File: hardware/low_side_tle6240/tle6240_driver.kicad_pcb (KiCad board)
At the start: 2 copper layers, 58.4 x 50.8 mm, 17 parts, among them K1 CONN_3, P1 CONN_10X2, P2 CONN_2, P3 CONN_4, P4 CONN_4, P5 CONN_4, P6 CONN_4

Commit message: v2
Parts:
- removed ? (x4): , 1pin
- removed P4, P5, P6: CONN_4, bornier4
- added K2: CONN_3, bornier3, F.Cu at (197.5, 97.2)
- added R3: R, SM0805, F.Cu at (186.7, 105.4)
- P2: value CONN_2 -> CONN_16; footprint bornier2 -> SIL-16_3.5MM
- P3: value CONN_4 -> CONN_2X2; footprint bornier4 -> PIN_ARRAY_2X2
- moved P2 130.4 mm to (217.2, 121.9), turned to 270 degrees
- moved C1 130.3 mm to (211.5, 142.2)
- moved K1 123.9 mm to (208.9, 143.5), turned to 90 degrees
- moved P3 102.9 mm to (195.6, 108.0), turned to 0 degrees
- moved R1 100.8 mm to (193.7, 102.9)
- moved D1 98.6 mm to (186.7, 103.5)
- moved D2 98.4 mm to (198.8, 132.1), turned to 180 degrees
- moved P1 72.6 mm to (179.1, 138.4)
- moved R2 54.3 mm to (188.0, 109.9), turned to 270 degrees
- moved D3 49.5 mm to (186.7, 107.3), turned to 0 degrees
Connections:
- D3 pad 1: N-0000034 -> +5V
- D3 pad 2: /Fault -> N-0000015
- P1 pad 1: +5V -> GND
- P1 pad 10: /SCLK -> /IN2
- P1 pad 11: /SO -> (no net)
- P1 pad 12: /CS -> /IN1
- P1 pad 13: /Reset -> (no net)
- P1 pad 14: /PRG -> /IN9
- P1 pad 15: /Fault -> /CS
- P1 pad 16: (no net) -> /IN10
- P1 pad 17: /IN4 -> /IN3
- P1 pad 18: /IN3 -> /IN11
- P1 pad 19: /IN10 -> /IN4
- P1 pad 2: +5V -> GND
- P1 pad 20: /IN9 -> /IN12
- P1 pad 3: GND -> +5V
- P1 pad 4: GND -> +5V
- P1 pad 5: /IN12 -> /+3.3V
- P1 pad 6: /IN11 -> /+3.3V
- P1 pad 7: /IN2 -> (no net)
- P1 pad 8: /IN1 -> (no net)
- P1 pad 9: /SI -> (no net)
- P2 pad 1: +5V -> /OUT6
- P2 pad 2: GND -> /OUT5
- P3 pad 1: /OUT9 -> /SI
- P3 pad 2: /OUT10 -> /Reset
- P3 pad 3: /OUT1 -> /SO
- P3 pad 4: /OUT2 -> /SCLK
- R2 pad 1: N-0000034 -> N-0000015
- R2 pad 2: +5V -> /Fault
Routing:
- net /+3.3V: track 0.00 -> 48.3 mm
- net /PRG: track 55.4 -> 17.0 mm, vias 1 -> 0
- net GND: track 118.4 -> 150.6 mm, vias 4 -> 3
- net /OUT6: track 24.3 -> 55.9 mm
- net /OUT5: track 21.2 -> 52.2 mm
- net /SCLK: track 18.3 -> 48.2 mm, vias 0 -> 1
- net /OUT16: track 19.2 -> 49.0 mm
- net /OUT14: track 19.1 -> 48.5 mm
- net /OUT15: track 19.1 -> 47.6 mm
- net /OUT8: track 21.2 -> 48.0 mm
- net /SI: track 15.2 -> 41.3 mm, vias 0 -> 1
- net /OUT13: track 19.2 -> 44.7 mm
- net /IN4: track 40.7 -> 66.1 mm
- net /OUT7: track 24.3 -> 48.5 mm
- net /SO: track 15.5 -> 37.8 mm, vias 0 -> 1
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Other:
- board size 58.4 x 50.8 mm -> 47 x 58.9 mm
- net class Power added: clearance 0.154, trace_width 0.4, via_dia 0.889, via_drill 0.635
- net class power removed
- board text removed: "+ -"
- board text removed: "Fault"
- board text removed: "OUT1"
- board text removed: "OUT10"
- board text removed: "OUT11"
- board text removed: "OUT12"
- board text removed: "OUT13"
- board text removed: "OUT14"
- board text removed: "OUT15"
- board text removed: "OUT16"
- board text removed: "OUT2"
- board text removed: "OUT3"
- board text removed: "OUT4"
- board text removed: "OUT5"
- board text removed: "OUT6"
- board text removed: "OUT7"
- board text removed: "OUT8"
- board text removed: "OUT9"
- board text removed: "Power"
- board text removed: "Prg"

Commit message: 
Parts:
- K1: value CONN_3 -> JUMPER3
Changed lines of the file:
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@@
   (net 33 /SO)
   (net 34 GND)
-  (net 35 N-0000015)
-  (net 36 N-0000017)
+  (net 35 N-0000014)
+  (net 36 N-0000023)
   (net_class Default "This is the default net class."
     (clearance 0)
@@
     (uvia_drill 0.127)
     (add_net "")
+    (add_net N-0000014)
+    (add_net N-0000023)
   )
   (net_class Power ""
@@
     (add_net /SI)
     (add_net /SO)
-    (add_net N-0000015)
-    (add_net N-0000017)
   )
   (module SM0805 (layer F.Cu)
@@
     (pad 2 smd rect (at 0.9525 0 180) (size 0.889 1.397)
       (layers F.Cu F.Paste F.Mask)
-      (net 36 N-0000017)
+      (net 36 N-0000023)
     )
     (model smd/chip_cms.wrl
@@
     (pad 1 smd rect (at -0.9525 0 270) (size 0.889 1.397)
       (layers F.Cu F.Paste F.Mask)
-      (net 35 N-0000015)
+      (net 35 N-0000014)
     )
     (pad 2 smd rect (at 0.9525 0 270) (size 0.889 1.397)
@@
       (effects (font (size 1.016 1.016) (thickness 0.1524)))
     )
-    (fp_text value CONN_3 (at 0 -2.159 90) (layer F.SilkS) hide
+    (fp_text value JUMPER3 (at 0 -2.159 90) (layer F.SilkS) hide
       (effects (font (size 1.016 1.016) (thickness 0.1524)))
     )
@@
     (pad 2 smd rect (at 1.04902 0) (size 1.19888 1.19888)
       (layers F.Cu F.Paste F.Mask)
-      (net 36 N-0000017)
+      (net 36 N-0000023)
     )
   )
@@
     (pad 2 smd rect (at 1.04902 0) (size 1.19888 1.19888)
       (layers F.Cu F.Paste F.Mask)
-      (net 35 N-0000015)
-    )
-  )
+      (net 35 N-0000014)
+    )
+  )

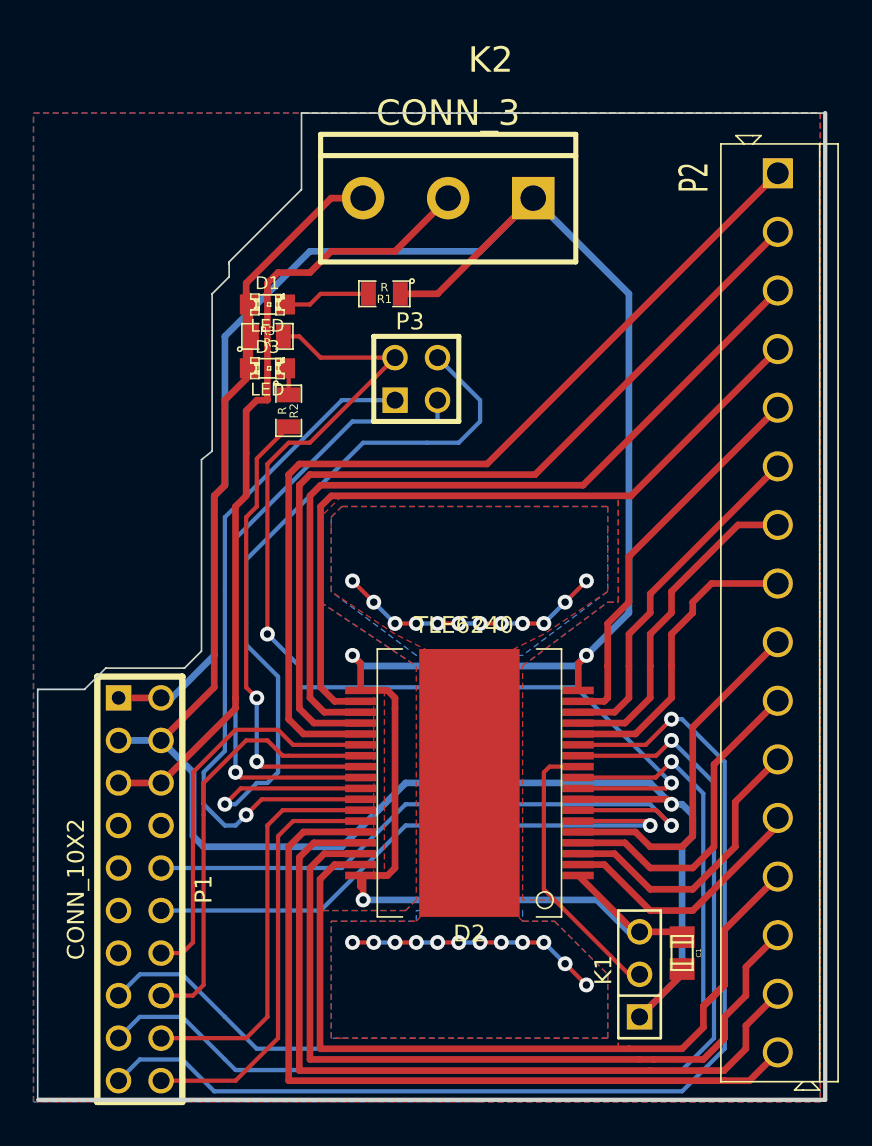
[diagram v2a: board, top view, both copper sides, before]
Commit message: 
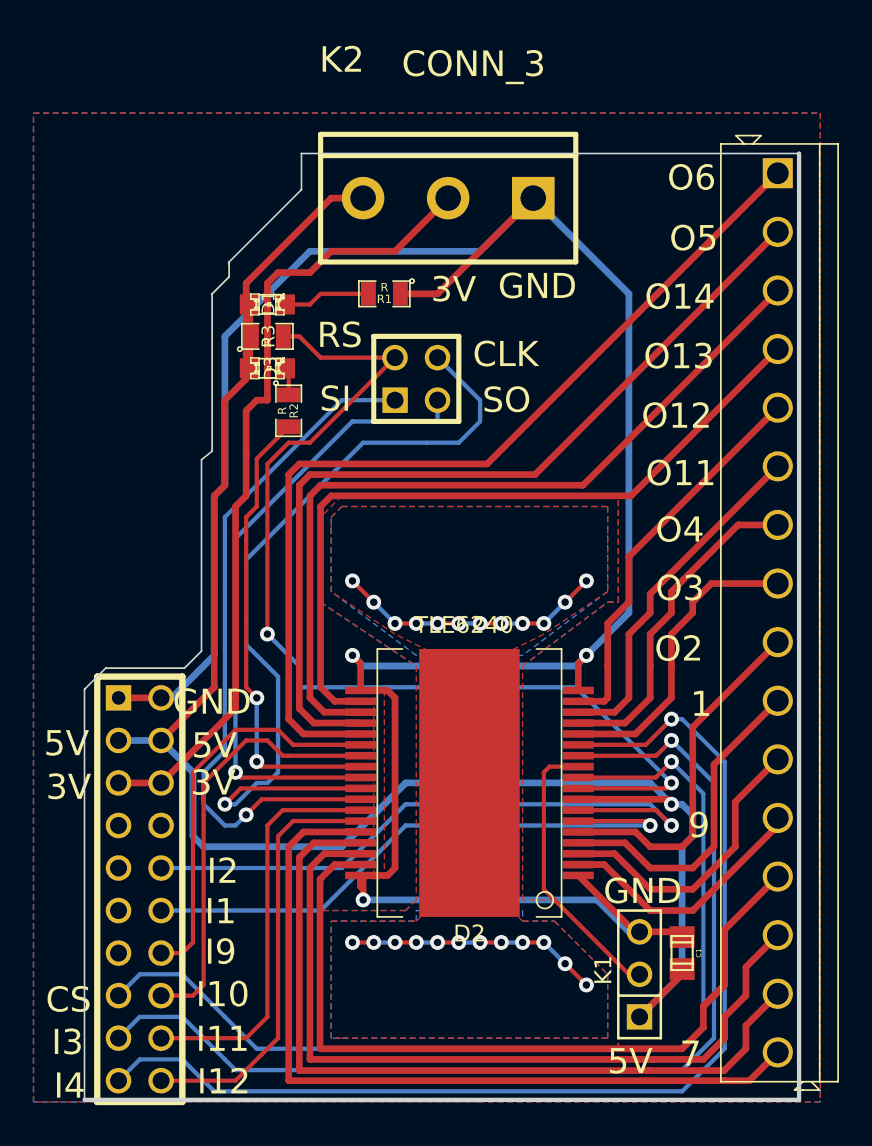
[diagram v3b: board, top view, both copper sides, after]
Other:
- board size 47 x 58.9 mm -> 42.7 x 56.5 mm
- board text added: "1"
- board text added: "3V"
- board text added: "5V"
- board text added: "7"
- board text added: "9"
- board text added: "CLK"
- board text added: "CS"
- board text added: "GND"
- board text added: "I1"
- board text added: "I10"
- board text added: "I11"
- board text added: "I12"
- board text added: "I2"
- board text added: "I3"
- board text added: "I4"
- board text added: "I9"
- board text added: "O11"
- board text added: "O12"
- board text added: "O13"
- board text added: "O14"
- board text added: "O2"
- board text added: "O3"
- board text added: "O4"
- board text added: "O5"
- board text added: "O6"
- board text added: "RS"
- board text added: "SI"
- board text added: "SO"
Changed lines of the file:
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@@
     (area 120.639999 87.8316 223.928 190.510001)
     (thickness 1.6)
-    (drawings 28)
+    (drawings 66)
     (tracks 403)
     (zones 0)
@@
     (visible_elements 7FFFFFFF)
     (pcbplotparams
-      (layerselection 317751297)
+      (layerselection 284983297)
       (usegerberextensions true)
       (excludeedgelayer true)
@@
       (drillshape 0)
       (scaleselection 1)
-      (outputdirectory gerber))
+      (outputdirectory gerber_tle6240))
   )
   (net 0 "")
@@
     (descr "Double rangee de contacts 2 x 10 pins")
     (tags CONN)
-    (fp_text reference P1 (at 0 -3.81 270) (layer F.SilkS)
+    (fp_text reference P1 (at 0 -3.81 270) (layer F.SilkS) hide
       (effects (font (size 1.016 1.016) (thickness 0.254)))
     )
-    (fp_text value CONN_10X2 (at 0 3.81 270) (layer F.SilkS)
+    (fp_text value CONN_10X2 (at -0.1905 7.747 270) (layer F.SilkS) hide
       (effects (font (size 1.016 1.016) (thickness 0.2032)))
     )
@@
     (tags "LED 0805 SMD")
     (attr smd)
-    (fp_text reference D1 (at 0 -1.27) (layer F.SilkS)
+    (fp_text reference D1 (at 0.0635 -0.0635 90) (layer F.SilkS)
       (effects (font (size 0.762 0.762) (thickness 0.127)))
     )
-    (fp_text value LED (at 0 1.27) (layer F.SilkS)
+    (fp_text value LED (at 0 1.27) (layer F.SilkS) hide
       (effects (font (size 0.762 0.762) (thickness 0.127)))
     )
@@
     (tags "LED 0805 SMD")
     (attr smd)
-    (fp_text reference D3 (at 0 -1.27) (layer F.SilkS)
+    (fp_text reference D3 (at 0.1905 0 90) (layer F.SilkS)
       (effects (font (size 0.762 0.762) (thickness 0.127)))
     )
-    (fp_text value LED (at 0 1.27) (layer F.SilkS)
+    (fp_text value LED (at 0 1.27) (layer F.SilkS) hide
       (effects (font (size 0.762 0.762) (thickness 0.127)))
     )
@@
     (descr "Bornier d'alimentation 3 pins")
     (tags DEV)
-    (fp_text reference K2 (at -2.54 8.255 180) (layer F.SilkS)
+    (fp_text reference K2 (at 6.35 8.255 180) (layer F.SilkS)
       (effects (font (size 1.524 1.524) (thickness 0.3048)))
     )
-    (fp_text value CONN_3 (at 0 5.08 180) (layer F.SilkS)
+    (fp_text value CONN_3 (at -1.524 8.001 180) (layer F.SilkS)
       (effects (font (size 1.524 1.524) (thickness 0.3048)))
     )
@@
     (at 217.17 121.92 270)
     (descr "14 PIN 3.5MM")
-    (fp_text reference P2 (at -26 5 270) (layer F.SilkS)
+    (fp_text reference P2 (at -28.5115 -5.3975 270) (layer F.SilkS) hide
       (effects (font (size 1.72974 1.08712) (thickness 0.27178)))
     )
@@
     (at 186.69 105.41)
     (attr smd)
-    (fp_text reference R3 (at 0 -0.3175) (layer F.SilkS)
-      (effects (font (size 0.50038 0.50038) (thickness 0.10922)))
+    (fp_text reference R3 (at 0.0635 0 90) (layer F.SilkS)
+      (effects (font (size 0.762 0.762) (thickness 0.10922)))
     )
     (fp_text value R (at 0 0.381) (layer F.SilkS)
@@
     (descr "Double rangee de contacts 2 x 2 pins")
     (tags CONN)
-    (fp_text reference P3 (at -0.381 -3.429) (layer F.SilkS)
+    (fp_text reference P3 (at -0.381 -3.429) (layer F.SilkS) hide
       (effects (font (size 1.016 1.016) (thickness 0.2032)))
     )
@@
     )
   )
-  (gr_line (start 219.964 92.075) (end 188.722 92.075) (angle 90) (layer Edge.Cuts) (width 0.1))
+  (gr_text GND (at 183.388 127.254) (layer F.SilkS)
+    (effects (font (size 1.5 1.5) (thickness 0.3)))
+  )
+  (gr_text 3V (at 183.515 132.08) (layer B.SilkS)
+    (effects (font (size 1.5 1.5) (thickness 0.3)) (justify mirror))
+  )
+  (gr_text 3V (at 183.4515 132.08) (layer F.SilkS)
+    (effects (font (size 1.5 1.5) (thickness 0.3)))
+  )
+  (gr_text 5V (at 183.515 129.8575) (layer B.SilkS)
+    (effects (font (size 1.5 1.5) (thickness 0.3)) (justify mirror))
+  )
+  (gr_text 5V (at 183.515 129.8575) (layer F.SilkS)
+    (effects (font (size 1.5 1.5) (thickness 0.3)))
+  )
+  (gr_text GND (at 209.1055 138.557) (layer F.SilkS)
+    (effects (font (size 1.5 1.5) (thickness 0.3)))
+  )
+  (gr_text 5V (at 208.3435 148.717) (layer F.SilkS)
+    (effects (font (size 1.5 1.5) (thickness 0.3)))
+  )
+  (gr_text 7 (at 211.963 148.2725) (layer F.SilkS)
+    (effects (font (size 1.5 1.5) (thickness 0.3)))
+  )
+  (gr_text 9 (at 212.471 134.62) (layer F.SilkS)
+    (effects (font (size 1.5 1.5) (thickness 0.3)))
+  )
+  (gr_text 1 (at 212.598 127.381) (layer F.SilkS)
+    (effects (font (size 1.5 1.5) (thickness 0.3)))
+  )
+  (gr_text O2 (at 211.2645 124.079) (layer B.SilkS)
+    (effects (font (size 1.5 1.5) (thickness 0.3)) (justify mirror))
+  )
+  (gr_text I2 (at 184.023 137.3505) (layer F.SilkS)
+    (effects (font (size 1.5 1.5) (thickness 0.3)))
+  )
+  (gr_text I1 (at 183.896 139.7635) (layer F.SilkS)
+    (effects (font (size 1.5 1.5) (thickness 0.3)))
+  )
+  (gr_text I9 (at 183.896 142.1765) (layer F.SilkS)
+    (effects (font (size 1.5 1.5) (thickness 0.3)))
+  )
+  (gr_text I10 (at 184.023 144.7165) (layer F.SilkS)
+    (effects (font (size 1.5 1.5) (thickness 0.3)))
+  )
+  (gr_text I11 (at 184.023 147.3835) (layer F.SilkS)
+    (effects (font (size 1.5 1.5) (thickness 0.3)))
+  )
+  (gr_text I12 (at 184.0865 149.9235) (layer F.SilkS)
+    (effects (font (size 1.5 1.5) (thickness 0.3)))
+  )
+  (gr_text CS (at 174.8155 145.034) (layer F.SilkS)
+    (effects (font (size 1.5 1.5) (thickness 0.3)))
+  )
+  (gr_text I3 (at 174.752 147.574) (layer F.SilkS)
+    (effects (font (size 1.5 1.5) (thickness 0.3)))
+  )
+  (gr_text I4 (at 174.879 150.1775) (layer F.SilkS)
+    (effects (font (size 1.5 1.5) (thickness 0.3)))
+  )
+  (gr_text 3V (at 174.8155 132.334) (layer F.SilkS)
+    (effects (font (size 1.5 1.5) (thickness 0.3)))
+  )
+  (gr_text 5V (at 174.6885 129.7305) (layer F.SilkS)
+    (effects (font (size 1.5 1.5) (thickness 0.3)))
+  )
+  (gr_text RS (at 191.008 105.3465) (layer F.SilkS)
+    (effects (font (size 1.5 1.5) (thickness 0.3)))
+  )
+  (gr_text SI (at 190.754 109.1565) (layer F.SilkS)
+    (effects (font (size 1.5 1.5) (thickness 0.3)))
+  )
+  (gr_text SO (at 200.9775 109.22) (layer F.SilkS)
+    (effects (font (size 1.5 1.5) (thickness 0.3)))
+  )
+  (gr_text CLK (at 200.914 106.4895) (layer F.SilkS)
+    (effects (font (size 1.5 1.5) (thickness 0.3)))
+  )
+  (gr_text 3V (at 197.866 102.616) (layer B.SilkS)
+    (effects (font (size 1.5 1.5) (thickness 0.3)) (justify mirror))
+  )
+  (gr_text 3V (at 197.8025 102.616) (layer F.SilkS)
+    (effects (font (size 1.5 1.5) (thickness 0.3)))
+  )
+  (gr_text GND (at 202.819 102.4255) (layer F.SilkS)
+    (effects (font (size 1.5 1.5) (thickness 0.3)))
+  )
+  (gr_text O2 (at 211.2645 124.079) (layer F.SilkS)
+    (effects (font (size 1.5 1.5) (thickness 0.3)))
+  )
+  (gr_text O3 (at 211.328 120.4595) (layer F.SilkS)
+    (effects (font (size 1.5 1.5) (thickness 0.3)))
+  )
+  (gr_text O4 (at 211.328 116.967) (layer F.SilkS)
+    (effects (font (size 1.5 1.5) (thickness 0.3)))
+  )
+  (gr_text O11 (at 211.3915 113.6015) (layer F.SilkS)
+    (effects (font (size 1.5 1.5) (thickness 0.3)))
+  )
+  (gr_text O12 (at 211.1375 110.1725) (layer F.SilkS)
+    (effects (font (size 1.5 1.5) (thickness 0.3)))
+  )
+  (gr_text O13 (at 211.2645 106.6165) (layer F.SilkS)
+    (effects (font (size 1.5 1.5) (thickness 0.3)))
+  )
+  (gr_text O14 (at 211.328 103.0605) (layer B.SilkS)
+    (effects (font (size 1.5 1.5) (thickness 0.3)) (justify mirror))
+  )
+  (gr_text O14 (at 211.328 103.0605) (layer F.SilkS)
+    (effects (font (size 1.5 1.5) (thickness 0.3)))
+  )
+  (gr_text O5 (at 212.1535 99.568) (layer F.SilkS)
+    (effects (font (size 1.5 1.5) (thickness 0.3)))
+  )
+  (gr_text O6 (at 212.0265 95.9485) (layer F.SilkS)
+    (effects (font (size 1.5 1.5) (thickness 0.3)))
+  )
+  (gr_line (start 218.44 94.488) (end 188.722 94.488) (angle 90) (layer Edge.Cuts) (width 0.1))
   (gr_line (start 177.038 125.222) (end 181.737 125.222) (angle 90) (layer Edge.Cuts) (width 0.1))
-  (gr_line (start 172.974 126.492) (end 175.768 126.492) (angle 90) (layer Edge.Cuts) (width 0.1))
-  (gr_line (start 220 92.075) (end 220 151.003) (angle 90) (layer Edge.Cuts) (width 0.254))
+  (gr_line (start 218.44 94.488) (end 218.44 151.003) (angle 90) (layer Edge.Cuts) (width 0.254))
   (gr_line (start 120.65 93.345) (end 186.69 93.345) (angle 90) (layer Eco2.User) (width 0.02))
   (gr_line (start 186.69 190.5) (end 186.69 93.472) (angle 90) (layer Eco2.User) (width 0.02))
@@
   (gr_line (start 127 187.96) (end 129.54 187.96) (angle 90) (layer Eco2.User) (width 0.02))
   (gr_line (start 127 127) (end 127 187.96) (angle 90) (layer Eco2.User) (width 0.02))
-  (gr_line (start 220 151.003) (end 173 151.003) (angle 90) (layer Edge.Cuts) (width 0.254))
+  (gr_line (start 218.44 151.003) (end 175.768 151.003) (angle 90) (layer Edge.Cuts) (width 0.254))
   (gr_line (start 177.038 125.222) (end 175.768 126.492) (angle 90) (layer Edge.Cuts) (width 0.1))
-  (gr_line (start 188.722 96.647) (end 188.722 92.075) (angle 90) (layer Edge.Cuts) (width 0.1))
+  (gr_line (start 188.722 96.647) (end 188.722 94.488) (angle 90) (layer Edge.Cuts) (width 0.1))
   (gr_line (start 184.404 100.965) (end 188.722 96.647) (angle 90) (layer Edge.Cuts) (width 0.1))
   (gr_line (start 184.404 101.092) (end 184.404 100.965) (angle 90) (layer Edge.Cuts) (width 0.1))
@@
   (gr_line (start 182.753 124.206) (end 182.753 112.776) (angle 90) (layer Edge.Cuts) (width 0.1))
   (gr_line (start 181.737 125.222) (end 182.753 124.206) (angle 90) (layer Edge.Cuts) (width 0.1))
-  (gr_line (start 172.974 151.003) (end 172.974 126.492) (angle 90) (layer Edge.Cuts) (width 0.1))
+  (gr_line (start 175.768 151.003) (end 175.768 126.492) (angle 90) (layer Edge.Cuts) (width 0.1))
   (via (at 191.77 120.015) (size 0.889) (layers F.Cu B.Cu) (net 0))
   (via (at 205.74 120.015) (size 0.889) (layers F.Cu B.Cu) (net 0))
